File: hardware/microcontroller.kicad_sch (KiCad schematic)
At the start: 22 parts, among them J5 1x2 jumper right-angle, J6 Conn_02x03_Odd_Even, J7 1x2 jumper right-angle, U1 74LVC2G125, U15 74LVC138A, U17 74LVC138A

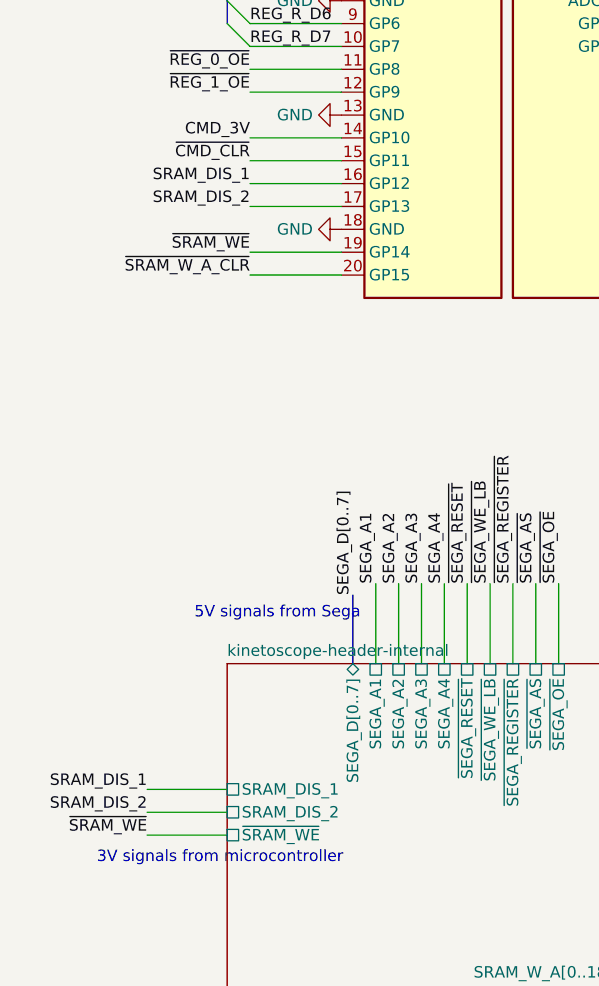
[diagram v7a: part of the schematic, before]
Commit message: Be consistent with SRAM bank numbering (0-1, not 1-2)
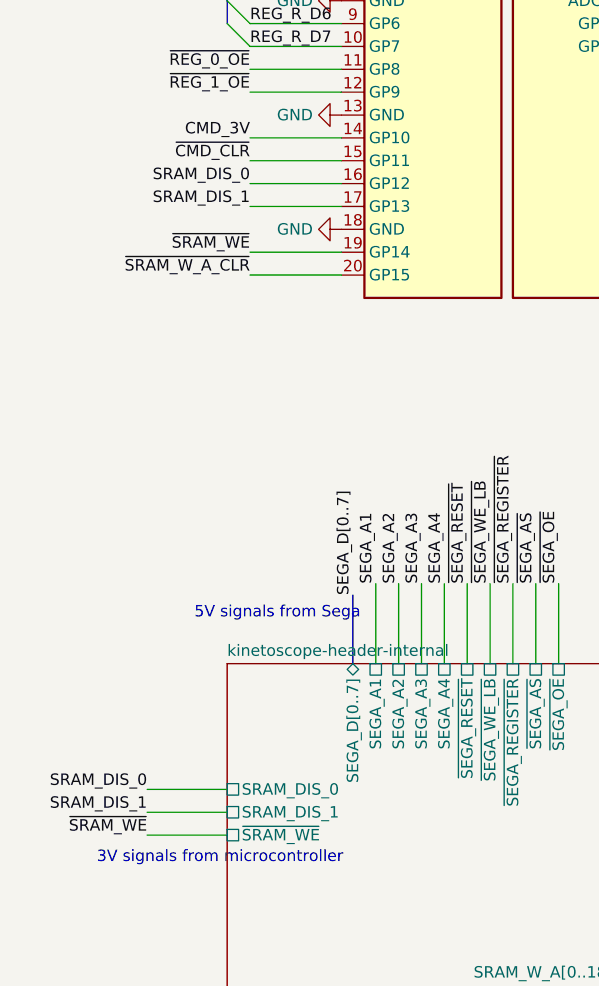
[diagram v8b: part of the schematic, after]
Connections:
- net SRAM_DIS_2 is gone; now on net SRAM_DIS_1: J3.17 (GP13)
- net SRAM_DIS_1: no longer J3.16 (GP12)
- new net SRAM_DIS_0: J3.16 (GP12)
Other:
- sheet kinetoscope-header-internal ports: added SRAM_DIS_0; removed SRAM_DIS_2
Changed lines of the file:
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@@
 		)
 	)
-	(label "SRAM_DIS_1"
+	(label "SRAM_DIS_0"
 		(at 24.13 156.21 180)
 		(fields_autoplaced yes)
@@
 		)
 	)
-	(label "SRAM_DIS_1"
+	(label "SRAM_DIS_0"
 		(at 35.56 88.9 180)
 		(fields_autoplaced yes)
@@
 		)
 	)
-	(label "SRAM_DIS_2"
+	(label "SRAM_DIS_1"
 		(at 35.56 91.44 180)
 		(fields_autoplaced yes)
@@
 		)
 	)
-	(label "SRAM_DIS_2"
+	(label "SRAM_DIS_1"
 		(at 24.13 158.75 180)
 		(fields_autoplaced yes)
@@
 			)
 		)
-		(pin "SRAM_DIS_2" passive
+		(pin "SRAM_DIS_1" passive
 			(at 33.02 158.75 180)
 			(effects
@@
 			)
 		)
-		(pin "SRAM_DIS_1" passive
+		(pin "SRAM_DIS_0" passive
 			(at 33.02 156.21 180)
 			(effects
